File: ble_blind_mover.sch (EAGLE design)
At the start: 56 parts, among them J1 105017-0001, Q1 DMG6968U-7, Q2 DMG6968U-7, U2 YJ-14015, U3 VIPER012LS, U4 MIC5205-3.3YM5-TR

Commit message: Aligned silkscreen labels
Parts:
- C1: value 10nF -> 10n
- C13, C2, C4: value 100nF -> 100n
- C18: value 470pF -> 470p
- C5: value 750pF -> 750p
- C6: value 22nF -> 22n
- C8, C9: value 120nF -> 120n
- L2: value 470uH -> 470u
- R1: value 15 -> 15R
- R10, R12, R8: value 470 -> 470R
- R16: value 0 -> 0R
- R3, R5: value 10 -> 10R
- renumbered D2 to LED1
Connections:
- net N$1 renamed U4_BYPASS
- new net SCL: U2.P0.10
- new net SDA: U2.P0.13
- net GO_UP: now also U2.P0.12; no longer U2.P0.13
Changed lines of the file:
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@@
 <?xml version="1.0" encoding="utf-8"?>
 <!DOCTYPE eagle SYSTEM "eagle.dtd">
-<eagle version="9.5.2">
+<eagle version="8.3.2">
 <drawing>
 <settings>
@@
 <parts>
 <part name="GND3" library="logic-supply" deviceset="GND" device=""/>
-<part name="C1" library="rcl" deviceset="C-EU" device="C0603" value="10nF"/>
-<part name="C2" library="rcl" deviceset="C-EU" device="C0603" value="100nF"/>
+<part name="C1" library="rcl" deviceset="C-EU" device="C0603" value="10n"/>
+<part name="C2" library="rcl" deviceset="C-EU" device="C0603" value="100n"/>
 <part name="C3" library="rcl" deviceset="C-EU" device="C0603" value="1uF"/>
 <part name="GND5" library="logic-supply" deviceset="GND" device=""/>
@@
 </part>
 <part name="D1" library="_hhn_diodes_smd" deviceset="SM400*" device="" technology="7"/>
-<part name="R1" library="rcl" deviceset="R-EU_" device="M1206" value="15"/>
+<part name="R1" library="rcl" deviceset="R-EU_" device="M1206" value="15R"/>
 <part name="C7" library="rcl" deviceset="C-EU" device="C0603" value="1uF"/>
 <part name="RELAY1" library="relay-relpol" deviceset="RM50-3011-XX-XXXX" device="" value="RM50-3011-85-1003">
@@
 <part name="Q2" library="SparkFun" deviceset="MOSFET-NCHANNEL" device="SMD" value="DMG6968U-7"/>
 <part name="R2" library="rcl" deviceset="R-EU_" device="R0603" value="47K"/>
-<part name="R3" library="rcl" deviceset="R-EU_" device="R0603" value="10"/>
+<part name="R3" library="rcl" deviceset="R-EU_" device="R0603" value="10R"/>
 <part name="R4" library="rcl" deviceset="R-EU_" device="R0603" value="47K"/>
-<part name="R5" library="rcl" deviceset="R-EU_" device="R0603" value="10"/>
+<part name="R5" library="rcl" deviceset="R-EU_" device="R0603" value="10R"/>
 <part name="GND6" library="logic-supply" deviceset="GND" device=""/>
 <part name="GND7" library="logic-supply" deviceset="GND" device=""/>
 <part name="R6" library="rcl" deviceset="R-EU_" device="R0603" value="TBD"/>
 <part name="R7" library="rcl" deviceset="R-EU_" device="R0603" value="TBD"/>
-<part name="R10" library="rcl" deviceset="R-EU_" device="R0603" value="470">
+<part name="R10" library="rcl" deviceset="R-EU_" device="R0603" value="470R">
 <attribute name="OC_TME" value="SMD0603-470R"/>
 </part>
-<part name="R8" library="rcl" deviceset="R-EU_" device="R0603" value="470">
+<part name="R8" library="rcl" deviceset="R-EU_" device="R0603" value="470R">
 <attribute name="OC_TME" value="SMD0603-470R"/>
 </part>
-<part name="D2" library="Wurth_Elektronik_Optoelectronics_rev15b" deviceset="WL-SFTW" device="-150141M173100-R&amp;G&amp;B"/>
+<part name="LED1" library="Wurth_Elektronik_Optoelectronics_rev15b" deviceset="WL-SFTW" device="-150141M173100-R&amp;G&amp;B"/>
 <part name="+3V6" library="supply1" deviceset="+3V3" device=""/>
-<part name="R12" library="rcl" deviceset="R-EU_" device="R0603" value="470">
+<part name="R12" library="rcl" deviceset="R-EU_" device="R0603" value="470R">
 <attribute name="OC_TME" value="SMD0603-470R"/>
 </part>
@@
 <part name="R11" library="rcl" deviceset="R-EU_" device="R0603" value="82K"/>
 <part name="R13" library="rcl" deviceset="R-EU_" device="R0603" value="47K"/>
-<part name="C4" library="rcl" deviceset="C-EU" device="C0603" value="100nF"/>
-<part name="C5" library="rcl" deviceset="C-EU" device="C0603" value="750pF"/>
+<part name="C4" library="rcl" deviceset="C-EU" device="C0603" value="100n"/>
+<part name="C5" library="rcl" deviceset="C-EU" device="C0603" value="750p"/>
 <part name="R14" library="rcl" deviceset="R-EU_" device="R0603" value="100K"/>
-<part name="C6" library="rcl" deviceset="C-EU" device="C0603" value="22nF"/>
-<part name="L2" library="SparkFun" deviceset="INDUCTOR" device="1210" value="470uH">
+<part name="C6" library="rcl" deviceset="C-EU" device="C0603" value="22n"/>
+<part name="L2" library="SparkFun" deviceset="INDUCTOR" device="1210" value="470u">
 <attribute name="OC_TME" value="NLV10JT471"/>
 </part>
-<part name="C8" library="rcl" deviceset="C-EU" device="150-064X183" value="120nF">
+<part name="C8" library="rcl" deviceset="C-EU" device="150-064X183" value="120n">
 <attribute name="OC_TME" value="MPP-120NR15/630"/>
 </part>
-<part name="C9" library="rcl" deviceset="C-EU" device="150-064X183" value="120nF">
+<part name="C9" library="rcl" deviceset="C-EU" device="150-064X183" value="120n">
 <attribute name="OC_TME" value="MPP-120NR15/630"/>
 </part>
@@
 <part name="S4" library="switch-omron" deviceset="10-XX" device=""/>
 <part name="FRAME4" library="martonmiklos" deviceset="A4L-LOC" device=""/>
-<part name="C13" library="rcl" deviceset="C-EU" device="C0603" value="100nF"/>
+<part name="C13" library="rcl" deviceset="C-EU" device="C0603" value="100n"/>
 <part name="C14" library="rcl" deviceset="C-EU" device="C0603" value="TBD"/>
 <part name="AGND1" library="supply1" deviceset="NEUTRAL" device=""/>
@@
 <part name="C16" library="rcl" deviceset="C-EU" device="C0603" value="1uF"/>
 <part name="C17" library="rcl" deviceset="C-EU" device="C0603" value="1uF"/>
-<part name="C18" library="rcl" deviceset="C-EU" device="C0603" value="470pF"/>
+<part name="C18" library="rcl" deviceset="C-EU" device="C0603" value="470p"/>
 <part name="GND16" library="logic-supply" deviceset="GND" device=""/>
 <part name="P+3" library="supply1" deviceset="+5V" device=""/>
@@
 <attribute name="NI_PN" value="715929-01"/>
 </part>
-<part name="R16" library="rcl" deviceset="R-EU_" device="0207/7" value="0"/>
+<part name="R16" library="rcl" deviceset="R-EU_" device="0207/7" value="0R"/>
 <part name="AGND3" library="supply1" deviceset="NEUTRAL" device=""/>
 <part name="AGND4" library="supply1" deviceset="NEUTRAL" device=""/>
@@
 <attribute name="OC_TME" x="213.36" y="137.16" size="1.778" layer="96" display="off"/>
 </instance>
-<instance part="D2" gate="G$1" x="198.12" y="144.78" smashed="yes">
+<instance part="LED1" gate="G$1" x="198.12" y="144.78" smashed="yes">
 <attribute name="NAME" x="196.97" y="156.622" size="1.27" layer="95" font="vector" ratio="10"/>
 <attribute name="VALUE" x="194.43" y="130.812" size="1.27" layer="96" font="vector" ratio="10"/>
@@
 <net name="+3V3" class="4">
 <segment>
-<pinref part="D2" gate="G$1" pin="A"/>
+<pinref part="LED1" gate="G$1" pin="A"/>
 <pinref part="+3V6" gate="G$1" pin="+3V3"/>
 <wire x1="187.96" y1="144.78" x2="180.34" y2="144.78" width="0.1524" layer="91"/>
@@
 <net name="GO_UP" class="4">
 <segment>
-<pinref part="U2" gate="G$1" pin="P0.13"/>
-<wire x1="157.48" y1="78.74" x2="162.56" y2="78.74" width="0.1524" layer="91"/>
-<label x="162.56" y="78.74" size="1.27" layer="95" font="vector" xref="yes"/>
-</segment>
-<segment>
 <pinref part="R3" gate="G$1" pin="1"/>
 <wire x1="78.74" y1="124.46" x2="76.2" y2="124.46" width="0.1524" layer="91"/>
 <label x="76.2" y="124.46" size="1.27" layer="95" font="vector" ratio="10" rot="R180" xref="yes"/>
 </segment>
+<segment>
+<pinref part="U2" gate="G$1" pin="P0.12"/>
+<wire x1="157.48" y1="76.2" x2="162.56" y2="76.2" width="0.1524" layer="91"/>
+<label x="162.56" y="76.2" size="1.27" layer="95" font="vector" xref="yes"/>
+</segment>
 </net>
 <net name="LED_R" class="4">
@@
 <segment>
 <pinref part="R8" gate="G$1" pin="1"/>
-<pinref part="D2" gate="G$1" pin="BC"/>
+<pinref part="LED1" gate="G$1" pin="BC"/>
 <wire x1="208.28" y1="137.16" x2="203.2" y2="137.16" width="0.1524" layer="91"/>
 </segment>
@@
 <segment>
 <pinref part="R10" gate="G$1" pin="1"/>
-<pinref part="D2" gate="G$1" pin="RC"/>
+<pinref part="LED1" gate="G$1" pin="RC"/>
 <wire x1="208.28" y1="144.78" x2="203.2" y2="144.78" width="0.1524" layer="91"/>
 </segment>
@@
 <segment>
 <pinref part="R12" gate="G$1" pin="1"/>
-<pinref part="D2" gate="G$1" pin="GC"/>
+<pinref part="LED1" gate="G$1" pin="GC"/>
 <wire x1="208.28" y1="152.4" x2="203.2" y2="152.4" width="0.1524" layer="91"/>
 </segment>
@@
 </segment>
 </net>
-<net name="N$1" class="4">
+<net name="U4_BYPASS" class="4">
 <segment>
 <pinref part="U4" gate="A" pin="BYP"/>
@@
 </segment>
 </net>
+<net name="SCL" class="0">
+<segment>
+<pinref part="U2" gate="G$1" pin="P0.10"/>
+<wire x1="142.24" y1="58.42" x2="142.24" y2="55.88" width="0.1524" layer="91"/>
+<label x="142.24" y="55.88" size="1.27" layer="95" font="vector" rot="R270" xref="yes"/>
+</segment>
+</net>
+<net name="SDA" class="4">
+<segment>
+<pinref part="U2" gate="G$1" pin="P0.13"/>
+<wire x1="157.48" y1="78.74" x2="162.56" y2="78.74" width="0.1524" layer="91"/>
+<label x="162.56" y="78.74" size="1.27" layer="95" font="vector" xref="yes"/>
+</segment>
+</net>

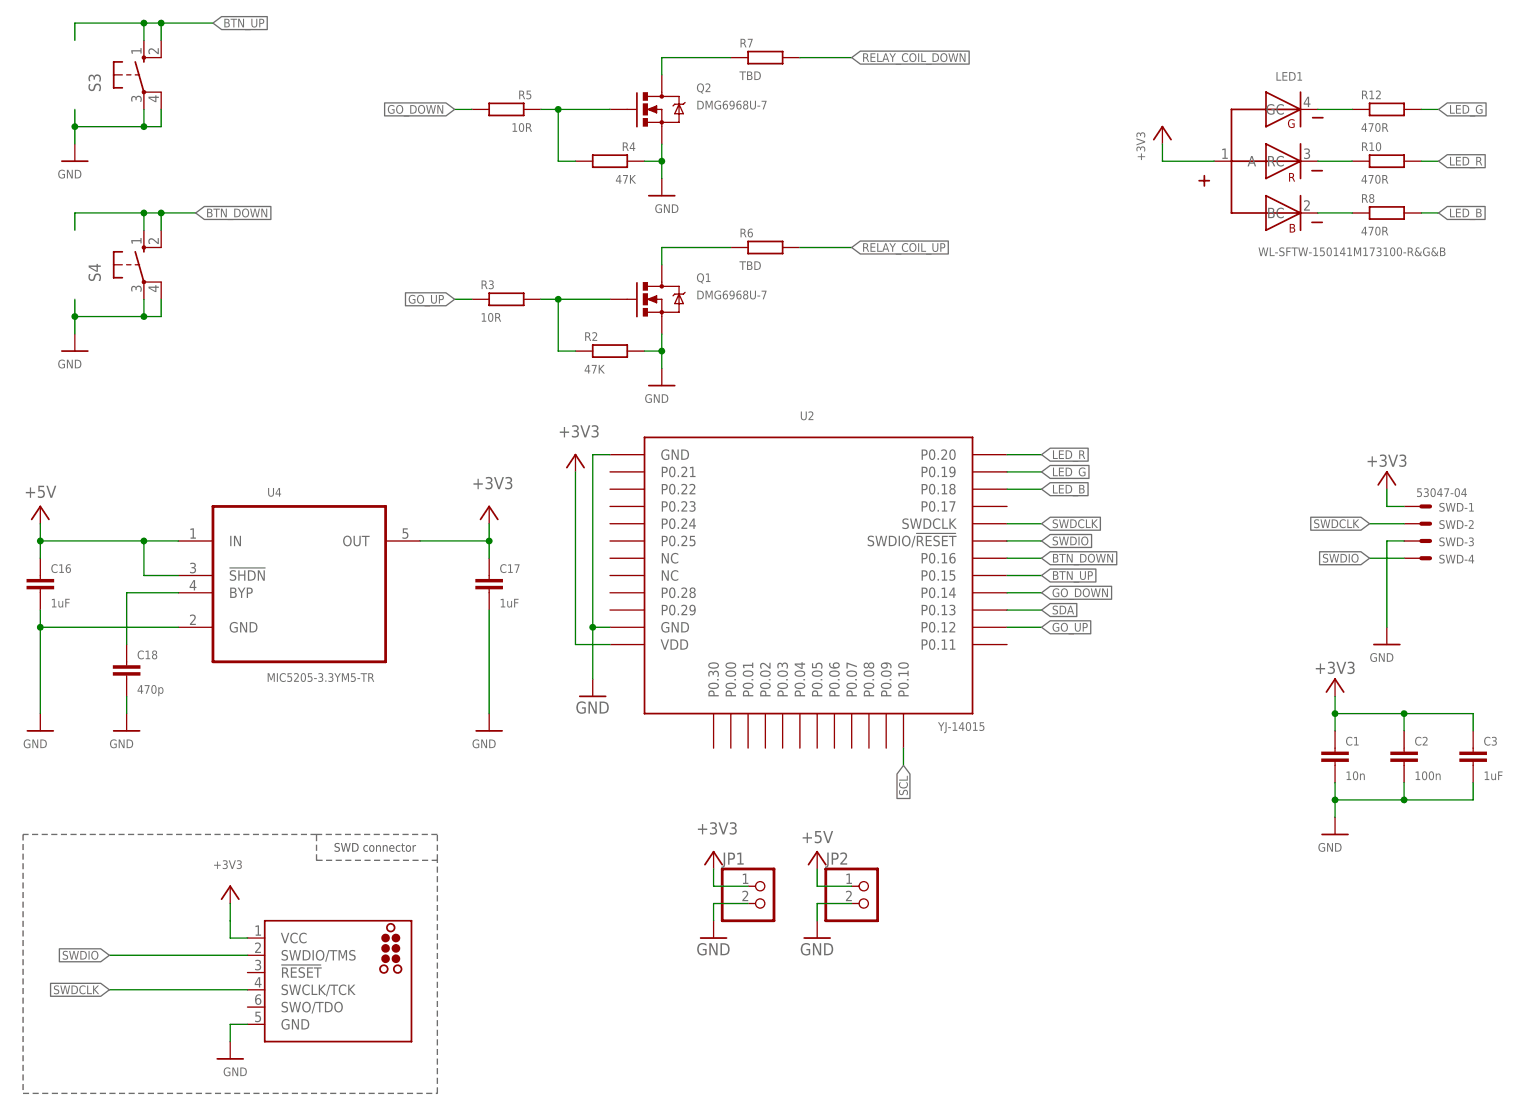
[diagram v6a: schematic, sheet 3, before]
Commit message: Added RTC
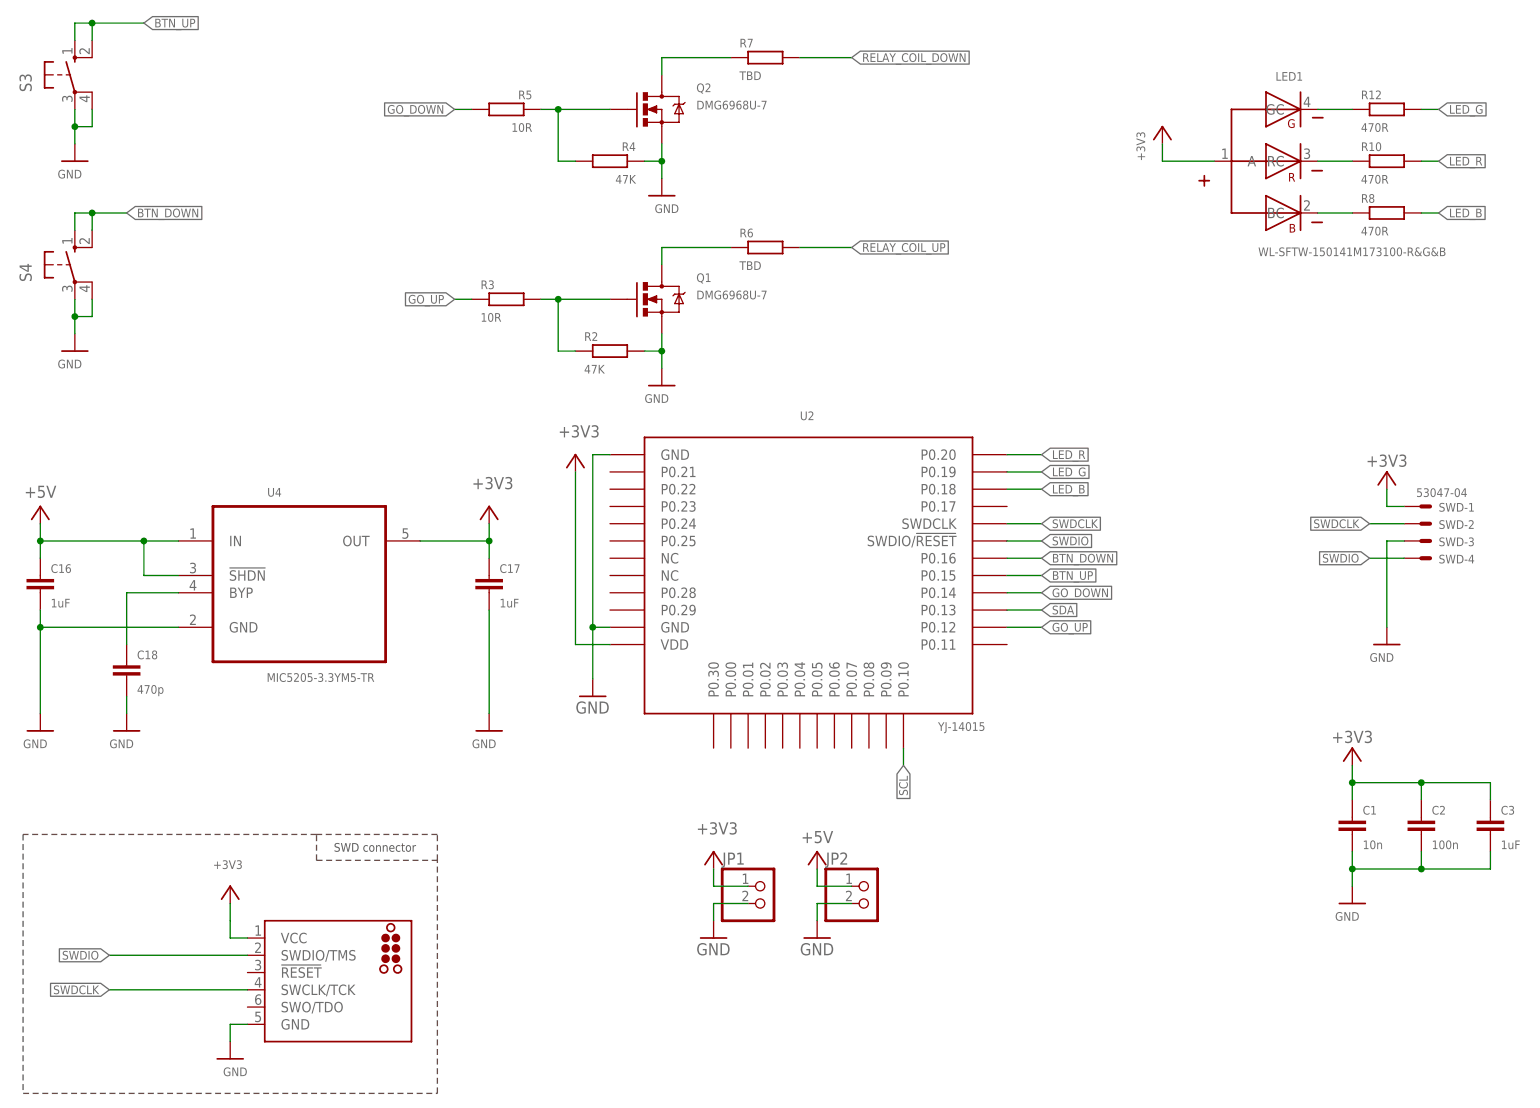
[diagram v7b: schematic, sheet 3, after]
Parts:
- added C12: 10n, rcl:C-EUC0603
- added C15: 100n, rcl:C-EUC0603
- added C19: 1uF, rcl:C-EUC0603
- added JP3: (no value), pinhead:PINHD-1X2
- added R15, R17: 4K7, rcl:R-EU_R0603
- added U1: MCP7940N-I/SN, MCP7940N-I_SN:MCP7940N-I/SN
- added Y1: LFXTAL016178, LFXTAL016178:LFXTAL016178
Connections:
- new net RTC_XTAL1: U1.X1, Y1.CRYSTAL_1
- new net RTC_XTAL2: U1.X2, Y1.CRYSTAL_2
- new net VBAT: JP3.1, U1.VBAT
- net +3V3: now also C12.1, C15.1, C19.1, R15.2, R17.2, U1.VCC
- net GND: now also C12.2, C15.2, C19.2, JP3.2, U1.VSS
- net SCL: now also R17.1, U1.SCL
- net SDA: now also R15.1, U1.SDA
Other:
- moved on the sheet: C1, C2, C3, S3, S4

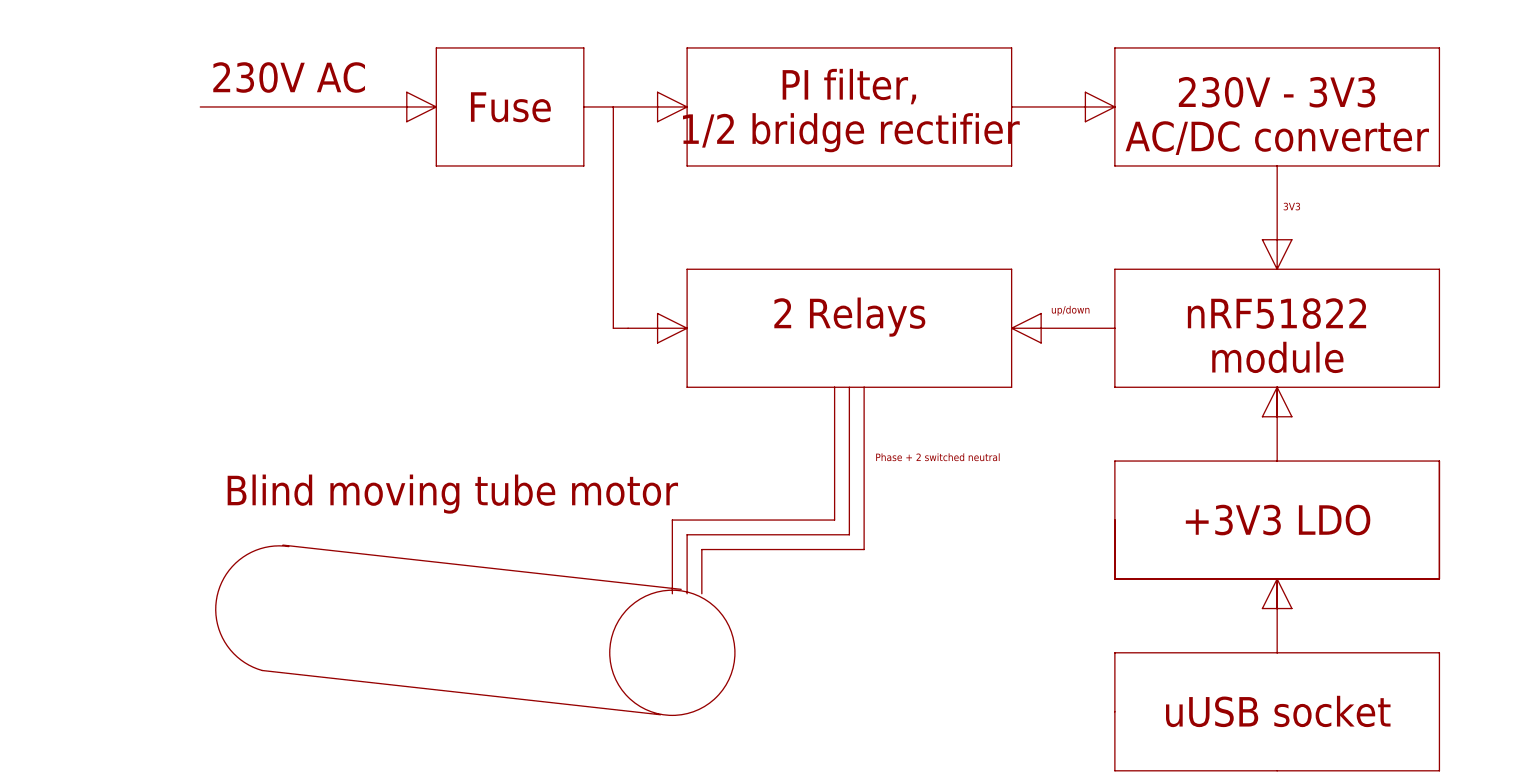
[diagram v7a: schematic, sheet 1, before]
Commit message: - Add RTC to cover page - Add schematic PDF to the repo
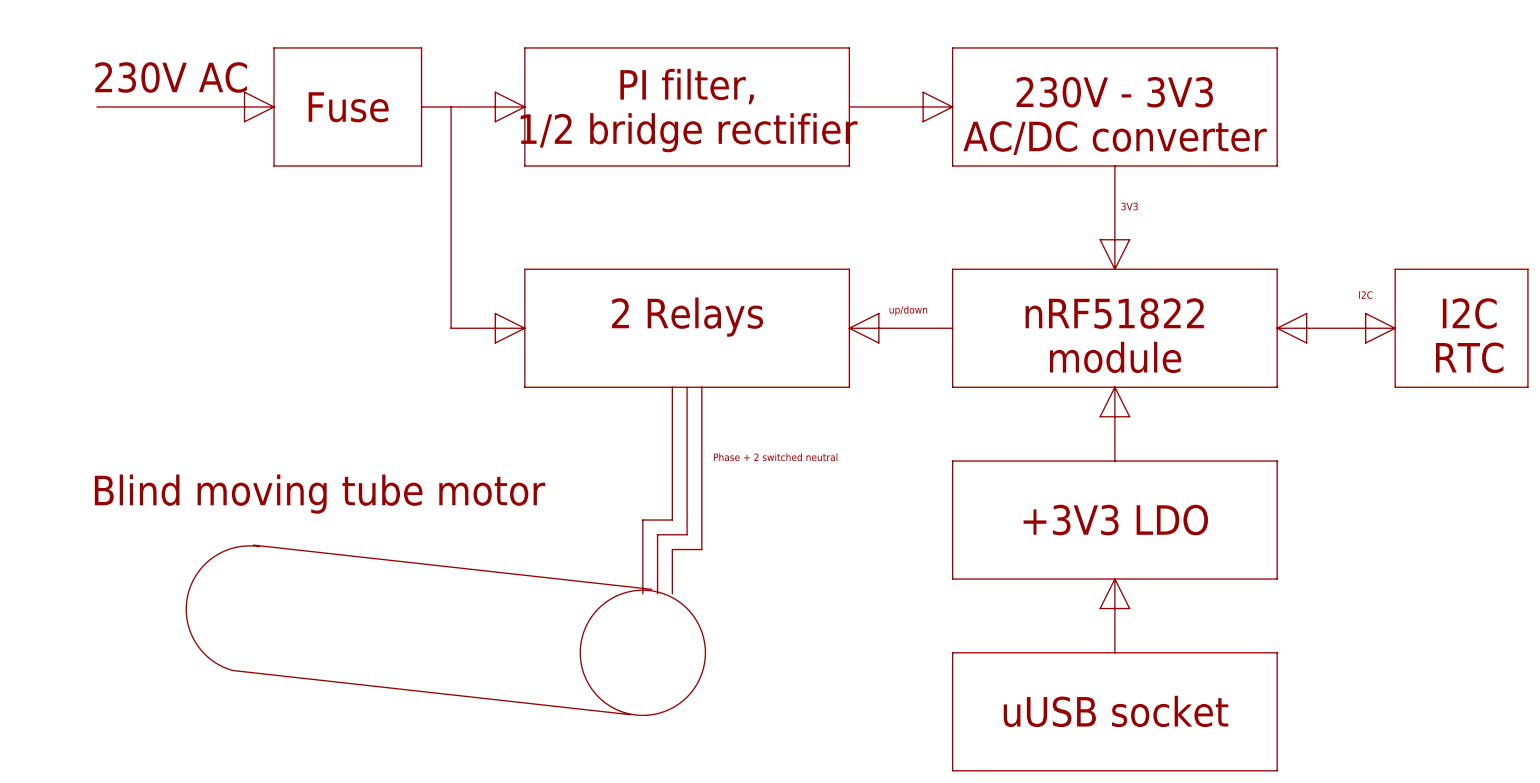
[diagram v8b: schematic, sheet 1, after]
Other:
- note added: "I2C"
- note added: "I2C RTC"
